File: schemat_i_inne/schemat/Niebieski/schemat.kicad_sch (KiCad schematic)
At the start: 36 parts, among them J1 Hole1, J2 Hole2, J3 Hole3, J4 Hole4, J5 programming port, J6 USB_B_Micro, SW1 SW_DIP_x01, SW2 Home, SW3 triggerR, SW4 Select, SW5 triggerL, SW6 BumperL, SW7 BumperR, U1 ATmega1284P, U2 L7805, U3 WG12864B-STBL, U4 LF33_TO252, U5 SN74LS07, U6 SD, Y1 16Mhz

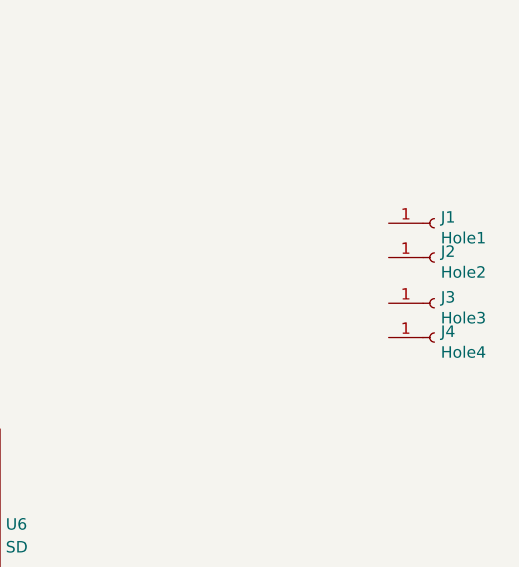
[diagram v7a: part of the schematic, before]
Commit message: Complete board, DRC test passed
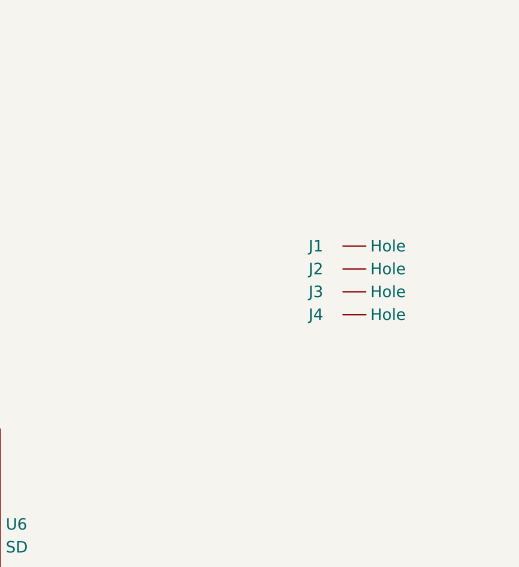
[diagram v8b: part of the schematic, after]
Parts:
- removed J1: Hole1, Connector_PinHeader_2.54mm:PinHeader_1x01_P2.54mm_Vertical, symbol Connector:Conn_01x01_Female
- removed J2: Hole2, Connector_PinHeader_2.54mm:PinHeader_1x01_P2.54mm_Vertical, symbol Connector:Conn_01x01_Female
- removed J3: Hole3, Connector_PinHeader_2.54mm:PinHeader_1x01_P2.54mm_Vertical, symbol Connector:Conn_01x01_Female
- removed J4: Hole4, Connector_PinHeader_2.54mm:PinHeader_1x01_P2.54mm_Vertical, symbol Connector:Conn_01x01_Female
- added J1, J2, J3, J4: ~, Holes:One_hole, symbol Holes:One_hole
- D1: footprint Diode_SMD:D_0201_0603Metric -> Diode_SMD:D_0603_1608Metric
- J6: footprint Connector_USB:USB_Micro-AB_Molex_47590-0001 -> USB:microUSB
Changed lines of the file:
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@@
-    )
-  )
-  (symbol (lib_id "Connector:Conn_01x01_Female") (at 269.24 53.34 0) (unit 1)
-    (in_bom yes) (on_board yes) (dnp no)
-    (property "Reference" "J1" (at 269.9512 52.6796 0)
-      (effects (font (size 1.27 1.27)) (justify left))
-    )
-    (property "Value" "Hole1" (at 269.9512 54.991 0)
-      (effects (font (size 1.27 1.27)) (justify left))
-    )
-    (property "Footprint" "Connector_PinHeader_2.54mm:PinHeader_1x01_P2.54mm_Vertical" (at 269.24 53.34 0)
-      (effects (font (size 1.27 1.27)) hide)
-    )
-    (property "Datasheet" "~" (at 269.24 53.34 0)
-      (effects (font (size 1.27 1.27)) hide)
-    )
-    (pin "1")
-    (instances
-      (project "schemat"
-        (path "/275aa44a-b61f-489f-9e2a-819a0fe0d1eb"
-          (reference "J1") (unit 1)
-        )
-      )
-    )
-  )
-  (symbol (lib_id "Connector:Conn_01x01_Female") (at 269.24 57.15 0) (unit 1)
-    (in_bom yes) (on_board yes) (dnp no)
-    (property "Reference" "J2" (at 269.9512 56.4896 0)
-      (effects (font (size 1.27 1.27)) (justify left))
-    )
-    (property "Value" "Hole2" (at 269.9512 58.801 0)
-      (effects (font (size 1.27 1.27)) (justify left))
-    )
-    (property "Footprint" "Connector_PinHeader_2.54mm:PinHeader_1x01_P2.54mm_Vertical" (at 269.24 57.15 0)
-      (effects (font (size 1.27 1.27)) hide)
-    )
-    (property "Datasheet" "~" (at 269.24 57.15 0)
-      (effects (font (size 1.27 1.27)) hide)
-    )
-    (pin "1")
-    (instances
-      (project "schemat"
-        (path "/275aa44a-b61f-489f-9e2a-819a0fe0d1eb"
-          (reference "J2") (unit 1)
-        )
-      )
-    )
-  )
-  (symbol (lib_id "Connector:Conn_01x01_Female") (at 269.24 62.23 0) (unit 1)
-    (in_bom yes) (on_board yes) (dnp no)
-    (property "Reference" "J3" (at 269.9512 61.5696 0)
-      (effects (font (size 1.27 1.27)) (justify left))
-    )
-    (property "Value" "Hole3" (at 269.9512 63.881 0)
-      (effects (font (size 1.27 1.27)) (justify left))
-    )
-    (property "Footprint" "Connector_PinHeader_2.54mm:PinHeader_1x01_P2.54mm_Vertical" (at 269.24 62.23 0)
-      (effects (font (size 1.27 1.27)) hide)
-    )
-    (property "Datasheet" "~" (at 269.24 62.23 0)
-      (effects (font (size 1.27 1.27)) hide)
-    )
-    (pin "1")
-    (instances
-      (project "schemat"
-        (path "/275aa44a-b61f-489f-9e2a-819a0fe0d1eb"
-          (reference "J3") (unit 1)
-        )
-      )
-    )
-  )
-  (symbol (lib_id "Connector:Conn_01x01_Female") (at 269.24 66.04 0) (unit 1)
-    (in_bom yes) (on_board yes) (dnp no)
-    (property "Reference" "J4" (at 269.9512 65.3796 0)
-      (effects (font (size 1.27 1.27)) (justify left))
-    )
-    (property "Value" "Hole4" (at 269.9512 67.691 0)
-      (effects (font (size 1.27 1.27)) (justify left))
-    )
-    (property "Footprint" "Connector_PinHeader_2.54mm:PinHeader_1x01_P2.54mm_Vertical" (at 269.24 66.04 0)
-      (effects (font (size 1.27 1.27)) hide)
-    )
-    (property "Datasheet" "~" (at 269.24 66.04 0)
-      (effects (font (size 1.27 1.27)) hide)
-    )
-    (pin "1")
-    (instances
-      (project "schemat"
-        (path "/275aa44a-b61f-489f-9e2a-819a0fe0d1eb"
-          (reference "J4") (unit 1)
-        )
-      )
     )
   )
@@
       (effects (font (size 1.27 1.27)) (justify left))
     )
-    (property "Footprint" "Connector_USB:USB_Micro-AB_Molex_47590-0001" (at 105.41 177.8 0)
+    (property "Footprint" "USB:microUSB" (at 105.41 177.8 0)
       (effects (font (size 1.27 1.27)) hide)
     )
@@
       (effects (font (size 1.27 1.27)))
     )
-    (property "Footprint" "Diode_SMD:D_0201_0603Metric" (at 49.53 182.88 0)
+    (property "Footprint" "Diode_SMD:D_0603_1608Metric" (at 49.53 182.88 0)
       (effects (font (size 1.27 1.27)) hide)
     )
@@
         (path "/275aa44a-b61f-489f-9e2a-819a0fe0d1eb"
           (reference "SW4") (unit 1)
+        )
+      )
+    )
+  )
+  (symbol (lib_id "Holes:One_hole") (at 261.62 55.88 0) (unit 1)
+    (in_bom yes) (on_board yes) (dnp no)
+    (property "Reference" "J1" (at 255.27 55.88 0)
+      (effects (font (size 1.27 1.27)) (justify left))
+    )
+    (property "Value" "~" (at 261.62 55.88 0)
+      (effects (font (size 1.27 1.27)))
+    )
+    (property "Footprint" "Holes:One_hole" (at 261.62 55.88 0)
+      (effects (font (size 1.27 1.27)) hide)
+    )
+    (property "Datasheet" "" (at 261.62 55.88 0)
+      (effects (font (size 1.27 1.27)) hide)
+    )
+    (pin "")
+    (instances
+      (project "schemat"
+        (path "/275aa44a-b61f-489f-9e2a-819a0fe0d1eb"
+          (reference "J1") (unit 1)
+        )
+      )
+    )
+  )
+  (symbol (lib_name "One_hole_3") (lib_id "Holes:One_hole") (at 261.62 63.5 0) (unit 1)
+    (in_bom yes) (on_board yes) (dnp no)
+    (property "Reference" "J4" (at 255.27 63.5 0)
+      (effects (font (size 1.27 1.27)) (justify left))
+    )
+    (property "Value" "~" (at 261.62 63.5 0)
+      (effects (font (size 1.27 1.27)))
+    )
+    (property "Footprint" "Holes:One_hole" (at 261.62 63.5 0)
+      (effects (font (size 1.27 1.27)) hide)
+    )
+    (property "Datasheet" "" (at 261.62 63.5 0)
+      (effects (font (size 1.27 1.27)) hide)
+    )
+    (pin "")
+    (instances
+      (project "schemat"
+        (path "/275aa44a-b61f-489f-9e2a-819a0fe0d1eb"
+          (reference "J4") (unit 1)
         )
       )
@@
     )
   )
+  (symbol (lib_name "One_hole_2") (lib_id "Holes:One_hole") (at 261.62 60.96 0) (unit 1)
+    (in_bom yes) (on_board yes) (dnp no)
+    (property "Reference" "J3" (at 255.27 60.96 0)
+      (effects (font (size 1.27 1.27)) (justify left))
+    )
+    (property "Value" "~" (at 261.62 60.96 0)
+      (effects (font (size 1.27 1.27)))
+    )
+    (property "Footprint" "Holes:One_hole" (at 261.62 60.96 0)
+      (effects (font (size 1.27 1.27)) hide)
+    )
+    (property "Datasheet" "" (at 261.62 60.96 0)
+      (effects (font (size 1.27 1.27)) hide)
+    )
+    (pin "")
+    (instances
+      (project "schemat"
+        (path "/275aa44a-b61f-489f-9e2a-819a0fe0d1eb"
+          (reference "J3") (unit 1)
+        )
+      )
+    )
+  )
   (symbol (lib_name "+5V_7") (lib_id "power:+5V") (at 100.33 36.83 0) (unit 1)
     (in_bom yes) (on_board yes) (dnp no) (fields_autoplaced)
@@
         )
       )
+    )
+  )
+  (symbol (lib_name "One_hole_1") (lib_id "Holes:One_hole") (at 261.62 58.42 0) (unit 1)
+    (in_bom yes) (on_board yes) (dnp no)
+    (property "Reference" "J2" (at 255.27 58.42 0)
+      (effects (font (size 1.27 1.27)) (justify left))
+    )
+    (property "Value" "~" (at 261.62 58.42 0)
+      (effects (font (size 1.27 1.27)))
+    )
+    (property "Footprint" "Holes:One_hole" (at 261.62 58.42 0)
+      (effects (font (size 1.27 1.27)) hide)
+    )
+    (property "Datasheet" "" (at 261.62 58.42 0)
+      (effects (font (size 1.27 1.27)) hide)
+    )
+    (pin "")
+    (instances
+      (project "schemat"
+        (path "/275aa44a-b61f-489f-9e2a-819a0fe0d1eb"
+          (reference "J2") (unit 1)
+        )
+      )
